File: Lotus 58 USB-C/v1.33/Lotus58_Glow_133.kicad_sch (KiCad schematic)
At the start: 117 parts, among them J3 USB_C_Receptacle_USB2.0, P1 OLED, SW1 Kailh hotswap MX socket, SW10 Kailh hotswap MX socket, SW11 Kailh hotswap MX socket, SW12 Kailh hotswap MX socket, SW13 Kailh hotswap MX socket, SW14 Kailh hotswap MX socket, SW15 Kailh hotswap MX socket, SW16 Kailh hotswap MX socket, SW17 Kailh hotswap MX socket, SW18 Kailh hotswap MX socket, SW19 Kailh hotswap MX socket, SW2 Kailh hotswap MX socket, SW20 Kailh hotswap MX socket, SW21 Kailh hotswap MX socket, SW22 Kailh hotswap MX socket, SW23 Kailh hotswap MX socket, SW24 Kailh hotswap MX socket, SW25 Kailh hotswap MX socket, SW26 Kailh hotswap MX socket, SW27 Kailh hotswap MX socket, SW28 Kailh hotswap MX socket, SW29 Kailh hotswap MX socket, SW3 Kailh hotswap MX socket, SW30 Rotary_Encoder_Switch, SW31 Rotary_Encoder_Switch, SW32 MSK12C02, SW33 MSK12C02, SW4 Kailh hotswap MX socket, SW5 Kailh hotswap MX socket, SW6 Kailh hotswap MX socket, SW7 Kailh hotswap MX socket, SW8 Kailh hotswap MX socket, SW9 Kailh hotswap MX socket, U1 ProMicro, U2 SRV05-4

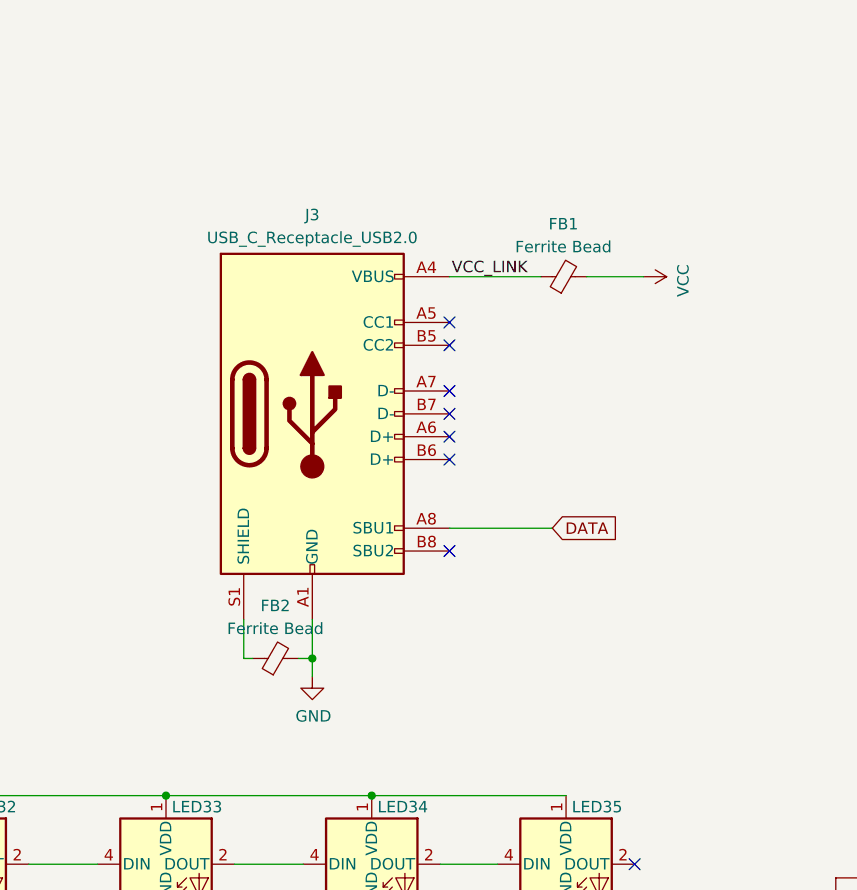
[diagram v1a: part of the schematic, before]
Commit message: Fixed silk screen inconsistencies
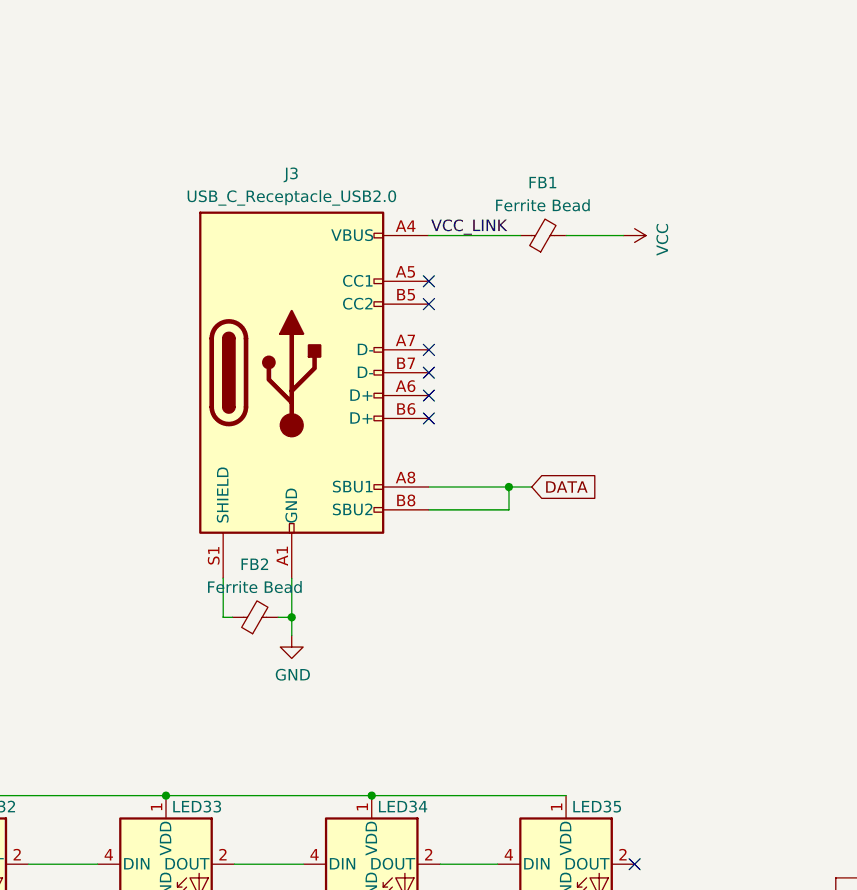
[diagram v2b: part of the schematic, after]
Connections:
- net DATA: now also J3.B8 (SBU2)
- no-connect marks 11 -> 10
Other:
- moved on the sheet: FB1, FB2, J3
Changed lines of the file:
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@@
   (junction (at 116.84 114.3) (diameter 0) (color 0 0 0 0)
   )
-  (junction (at 315.976 190.5) (diameter 0) (color 0 0 0 0)
+  (junction (at 313.69 185.928) (diameter 0) (color 0 0 0 0)
   )
   (junction (at 45.72 226.06) (diameter 0) (color 0 0 0 0)
@@
   (junction (at 96.52 64.77) (diameter 0) (color 0 0 0 0)
   )
+  (junction (at 337.82 171.45) (diameter 0) (color 0 0 0 0)
+  )
   (junction (at 43.18 73.66) (diameter 0) (color 0 0 0 0)
   )
@@
   )
   (no_connect (at 351.79 213.36))
-  (no_connect (at 331.216 163.322))
-  (no_connect (at 331.216 153.162))
-  (no_connect (at 331.216 168.402))
-  (no_connect (at 331.216 155.702))
-  (no_connect (at 331.216 178.562))
+  (no_connect (at 328.93 158.75))
+  (no_connect (at 328.93 148.59))
+  (no_connect (at 328.93 163.83))
+  (no_connect (at 328.93 151.13))
   (no_connect (at 226.06 122.174))
   (no_connect (at 251.46 117.094))
-  (no_connect (at 331.216 160.782))
-  (no_connect (at 331.216 165.862))
+  (no_connect (at 328.93 156.21))
+  (no_connect (at 328.93 161.29))
   (no_connect (at 354.33 63.5))
   (wire (pts (xy 354.33 81.28) (xy 359.41 81.28))
@@
     (stroke (width 0) (type default))
   )
-  (wire (pts (xy 308.356 186.182) (xy 308.356 190.5))
+  (wire (pts (xy 306.07 181.61) (xy 306.07 185.928))
     (stroke (width 0) (type default))
   )
@@
     (stroke (width 0) (type default))
   )
-  (wire (pts (xy 308.356 190.5) (xy 309.372 190.5))
+  (wire (pts (xy 306.07 185.928) (xy 307.086 185.928))
     (stroke (width 0) (type default))
   )
@@
     (stroke (width 0) (type default))
   )
-  (wire (pts (xy 315.976 192.532) (xy 315.976 190.5))
+  (wire (pts (xy 313.69 187.96) (xy 313.69 185.928))
     (stroke (width 0) (type default))
   )
@@
     (stroke (width 0) (type default))
   )
+  (wire (pts (xy 337.82 171.45) (xy 337.82 173.99))
+    (stroke (width 0) (type default))
+  )
   (wire (pts (xy 66.04 173.99) (xy 86.36 173.99))
     (stroke (width 0) (type default))
   )
-  (wire (pts (xy 352.806 148.082) (xy 346.456 148.082))
+  (wire (pts (xy 350.52 143.51) (xy 344.17 143.51))
     (stroke (width 0) (type default))
   )
@@
     (stroke (width 0) (type default))
   )
+  (wire (pts (xy 337.82 173.99) (xy 328.93 173.99))
+    (stroke (width 0) (type default))
+  )
   (wire (pts (xy 96.52 90.17) (xy 93.98 90.17))
     (stroke (width 0) (type default))
@@
     (stroke (width 0) (type default))
   )
+  (wire (pts (xy 337.82 171.45) (xy 340.36 171.45))
+    (stroke (width 0) (type default))
+  )
   (wire (pts (xy 127 245.11) (xy 127 243.84))
     (stroke (width 0) (type default))
@@
     (stroke (width 0) (type default))
   )
-  (wire (pts (xy 341.376 148.082) (xy 331.216 148.082))
+  (wire (pts (xy 339.09 143.51) (xy 328.93 143.51))
     (stroke (width 0) (type default))
   )
@@
     (stroke (width 0) (type default))
   )
-  (wire (pts (xy 314.452 190.5) (xy 315.976 190.5))
+  (wire (pts (xy 312.166 185.928) (xy 313.69 185.928))
     (stroke (width 0) (type default))
   )
@@
     (stroke (width 0) (type default))
   )
-  (wire (pts (xy 315.976 190.5) (xy 315.976 186.182))
+  (wire (pts (xy 313.69 185.928) (xy 313.69 181.61))
     (stroke (width 0) (type default))
   )
@@
     (stroke (width 0) (type default))
   )
-  (wire (pts (xy 331.216 176.022) (xy 342.646 176.022))
+  (wire (pts (xy 328.93 171.45) (xy 337.82 171.45))
     (stroke (width 0) (type default))
   )
@@
     (effects (font (size 1.27 1.27)) (justify left bottom))
   )
-  (label "VCC_LINK" (at 331.47 148.082 0) (fields_autoplaced)
+  (label "VCC_LINK" (at 329.184 143.51 0) (fields_autoplaced)
     (effects (font (size 1.27 1.27)) (justify left bottom))
   )
@@
     )
   )
-  (global_label "DATA" (shape input) (at 342.646 176.022 0) (fields_autoplaced)
+  (global_label "DATA" (shape input) (at 340.36 171.45 0) (fields_autoplaced)
     (effects (font (size 1.27 1.27)) (justify left))
-    (property "Intersheetrefs" "${INTERSHEET_REFS}" (at 349.3124 176.022 0)
+    (property "Intersheetrefs" "${INTERSHEET_REFS}" (at 347.0264 171.45 0)
       (effects (font (size 1.27 1.27)) (justify left) hide)
     )
@@
     )
   )
-  (symbol (lib_id "power:GND") (at 315.976 192.532 0) (unit 1)
+  (symbol (lib_id "power:GND") (at 313.69 187.96 0) (unit 1)
     (in_bom yes) (on_board yes) (dnp no)
-    (property "Reference" "#PWR011" (at 315.976 198.882 0)
+    (property "Reference" "#PWR011" (at 313.69 194.31 0)
       (effects (font (size 1.27 1.27)) hide)
     )
-    (property "Value" "GND" (at 316.103 196.9262 0)
+    (property "Value" "GND" (at 313.817 192.3542 0)
       (effects (font (size 1.27 1.27)))
     )
-    (property "Footprint" "" (at 315.976 192.532 0)
+    (property "Footprint" "" (at 313.69 187.96 0)
       (effects (font (size 1.27 1.27)) hide)
     )
-    (property "Datasheet" "" (at 315.976 192.532 0)
+    (property "Datasheet" "" (at 313.69 187.96 0)
       (effects (font (size 1.27 1.27)) hide)
     )
@@
     )
   )
-  (symbol (lib_id "power:VCC") (at 352.806 148.082 270) (unit 1)
+  (symbol (lib_id "power:VCC") (at 350.52 143.51 270) (unit 1)
     (in_bom yes) (on_board yes) (dnp no)
-    (property "Reference" "#PWR012" (at 348.996 148.082 0)
+    (property "Reference" "#PWR012" (at 346.71 143.51 0)
       (effects (font (size 1.27 1.27)) hide)
     )
-    (property "Value" "VCC" (at 357.2002 148.5138 0)
+    (property "Value" "VCC" (at 354.9142 143.9418 0)
       (effects (font (size 1.27 1.27)))
     )
-    (property "Footprint" "" (at 352.806 148.082 0)
+    (property "Footprint" "" (at 350.52 143.51 0)
       (effects (font (size 1.27 1.27)) hide)
     )
-    (property "Datasheet" "" (at 352.806 148.082 0)
+    (property "Datasheet" "" (at 350.52 143.51 0)
       (effects (font (size 1.27 1.27)) hide)
     )
@@
     )
   )
-  (symbol (lib_id "LCSC Parts:Ferrite Bead") (at 311.912 190.5 90) (unit 1)
+  (symbol (lib_id "LCSC Parts:Ferrite Bead") (at 309.626 185.928 90) (unit 1)
     (in_bom yes) (on_board yes) (dnp no) (fields_autoplaced)
-    (property "Reference" "FB2" (at 311.8739 184.658 90)
+    (property "Reference" "FB2" (at 309.5879 180.086 90)
       (effects (font (size 1.27 1.27)))
     )
-    (property "Value" "Ferrite Bead" (at 311.8739 187.198 90)
+    (property "Value" "Ferrite Bead" (at 309.5879 182.626 90)
       (effects (font (size 1.27 1.27)))
     )
-    (property "Footprint" "Capacitor_SMD:C_0603_1608Metric_Pad1.08x0.95mm_HandSolder" (at 311.912 192.278 90)
+    (property "Footprint" "Capacitor_SMD:C_0603_1608Metric_Pad1.08x0.95mm_HandSolder" (at 309.626 187.706 90)
       (effects (font (size 1.27 1.27)) hide)
     )
-    (property "Datasheet" "~" (at 311.912 190.5 0)
+    (property "Datasheet" "~" (at 309.626 185.928 0)
       (effects (font (size 1.27 1.27)) hide)
     )
-    (property "LCSC" "C882974" (at 311.912 190.5 0)
+    (property "LCSC" "C882974" (at 309.626 185.928 0)
       (effects (font (size 1.27 1.27)) hide)
     )
@@
     )
   )
-  (symbol (lib_id "Connector:USB_C_Receptacle_USB2.0") (at 315.976 163.322 0) (unit 1)
+  (symbol (lib_id "Connector:USB_C_Receptacle_USB2.0") (at 313.69 158.75 0) (unit 1)
     (in_bom yes) (on_board yes) (dnp no) (fields_autoplaced)
-    (property "Reference" "J3" (at 315.976 141.224 0)
+    (property "Reference" "J3" (at 313.69 136.652 0)
       (effects (font (size 1.27 1.27)))
     )
-    (property "Value" "USB_C_Receptacle_USB2.0" (at 315.976 143.764 0)
+    (property "Value" "USB_C_Receptacle_USB2.0" (at 313.69 139.192 0)
       (effects (font (size 1.27 1.27)))
     )
-    (property "Footprint" "LCSC_Library:Molex-216990_GCT-USB45xx_HRO-TYPE-C-31-M-13x-PiMicro" (at 319.786 163.322 0)
+    (property "Footprint" "LCSC_Library:Molex-216990_GCT-USB45xx_HRO-TYPE-C-31-M-13x-PiMicro" (at 317.5 158.75 0)
       (effects (font (size 1.27 1.27)) hide)
     )
-    (property "Datasheet" "https://www.usb.org/sites/default/files/documents/usb_type-c.zip" (at 319.786 163.322 0)
+    (property "Datasheet" "https://www.usb.org/sites/default/files/documents/usb_type-c.zip" (at 317.5 158.75 0)
       (effects (font (size 1.27 1.27)) hide)
     )
-    (property "LCSC" "C963373" (at 315.976 163.322 0)
+    (property "LCSC" "C963373" (at 313.69 158.75 0)
       (effects (font (size 1.27 1.27)) hide)
     )
@@
     )
   )
-  (symbol (lib_id "LCSC Parts:Ferrite Bead") (at 343.916 148.082 90) (unit 1)
+  (symbol (lib_id "LCSC Parts:Ferrite Bead") (at 341.63 143.51 90) (unit 1)
     (in_bom yes) (on_board yes) (dnp no) (fields_autoplaced)
-    (property "Reference" "FB1" (at 343.8779 142.24 90)
+    (property "Reference" "FB1" (at 341.5919 137.668 90)
       (effects (font (size 1.27 1.27)))
     )
-    (property "Value" "Ferrite Bead" (at 343.8779 144.78 90)
+    (property "Value" "Ferrite Bead" (at 341.5919 140.208 90)
       (effects (font (size 1.27 1.27)))
     )
-    (property "Footprint" "Capacitor_SMD:C_0603_1608Metric_Pad1.08x0.95mm_HandSolder" (at 343.916 149.86 90)
+    (property "Footprint" "Capacitor_SMD:C_0603_1608Metric_Pad1.08x0.95mm_HandSolder" (at 341.63 145.288 90)
       (effects (font (size 1.27 1.27)) hide)
     )
-    (property "Datasheet" "~" (at 343.916 148.082 0)
+    (property "Datasheet" "~" (at 341.63 143.51 0)
       (effects (font (size 1.27 1.27)) hide)
     )
-    (property "LCSC" "C882974" (at 343.916 148.082 0)
+    (property "LCSC" "C882974" (at 341.63 143.51 0)
       (effects (font (size 1.27 1.27)) hide)
     )
